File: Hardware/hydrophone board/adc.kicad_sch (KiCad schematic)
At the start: 25 parts, among them J301 Conn_01x08

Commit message: changed all cap + resistors to 0805, starting filter layout
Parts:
- C301, C302, C303, C305, C306, C308, C309, C310, C311, C312, C313, C314, C315, C316, C317, C318: footprint Capacitor_SMD:C_0603_1608Metric -> Capacitor_SMD:C_0805_2012Metric_Pad1.18x1.45mm_HandSolder
- C304, C307: footprint Capacitor_SMD:C_0805_2012Metric -> Capacitor_SMD:C_0805_2012Metric_Pad1.18x1.45mm_HandSolder
- R301, R302, R303, R304, R305: footprint Resistor_SMD:R_0603_1608Metric -> Resistor_SMD:R_0805_2012Metric_Pad1.20x1.40mm_HandSolder
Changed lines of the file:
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@@
       (effects (font (size 1.27 1.27)))
     )
-    (property "Footprint" "Capacitor_SMD:C_0603_1608Metric" (at 118.11 176.8348 0)
+    (property "Footprint" "Capacitor_SMD:C_0805_2012Metric_Pad1.18x1.45mm_HandSolder" (at 118.11 176.8348 0)
       (effects (font (size 1.27 1.27)) hide)
     )
@@
       (effects (font (size 1.27 1.27)) (justify left))
     )
-    (property "Footprint" "Capacitor_SMD:C_0603_1608Metric" (at 38.1 49.53 0)
+    (property "Footprint" "Capacitor_SMD:C_0805_2012Metric_Pad1.18x1.45mm_HandSolder" (at 38.1 49.53 0)
       (effects (font (size 1.27 1.27)) hide)
     )
@@
       (effects (font (size 1.27 1.27)) (justify left))
     )
-    (property "Footprint" "Resistor_SMD:R_0603_1608Metric" (at 242.316 101.854 90)
+    (property "Footprint" "Resistor_SMD:R_0805_2012Metric_Pad1.20x1.40mm_HandSolder" (at 242.316 101.854 90)
       (effects (font (size 1.27 1.27)) hide)
     )
@@
       (effects (font (size 1.27 1.27)) (justify left))
     )
-    (property "Footprint" "Capacitor_SMD:C_0603_1608Metric" (at 77.1652 53.34 0)
+    (property "Footprint" "Capacitor_SMD:C_0805_2012Metric_Pad1.18x1.45mm_HandSolder" (at 77.1652 53.34 0)
       (effects (font (size 1.27 1.27)) hide)
     )
@@
     (pin "18")
     (pin "19")
-    (pin "2")
     (pin "20")
     (pin "21")
@@
     (pin "8")
     (pin "9")
+    (pin "2")
     (instances
       (project "hydrophone board"
@@
       (effects (font (size 1.27 1.27)) (justify right))
     )
-    (property "Footprint" "Resistor_SMD:R_0603_1608Metric" (at 189.484 106.426 90)
+    (property "Footprint" "Resistor_SMD:R_0805_2012Metric_Pad1.20x1.40mm_HandSolder" (at 189.484 106.426 90)
       (effects (font (size 1.27 1.27)) hide)
     )
@@
       (effects (font (size 1.27 1.27)))
     )
-    (property "Footprint" "Capacitor_SMD:C_0603_1608Metric" (at 54.61 176.8348 0)
+    (property "Footprint" "Capacitor_SMD:C_0805_2012Metric_Pad1.18x1.45mm_HandSolder" (at 54.61 176.8348 0)
       (effects (font (size 1.27 1.27)) hide)
     )
@@
       (effects (font (size 1.27 1.27)) (justify left))
     )
-    (property "Footprint" "Capacitor_SMD:C_0603_1608Metric" (at 214.3252 64.77 0)
+    (property "Footprint" "Capacitor_SMD:C_0805_2012Metric_Pad1.18x1.45mm_HandSolder" (at 214.3252 64.77 0)
       (effects (font (size 1.27 1.27)) hide)
     )
@@
       (effects (font (size 1.27 1.27)) (justify left))
     )
-    (property "Footprint" "Capacitor_SMD:C_0603_1608Metric" (at 239.7252 57.15 0)
+    (property "Footprint" "Capacitor_SMD:C_0805_2012Metric_Pad1.18x1.45mm_HandSolder" (at 239.7252 57.15 0)
       (effects (font (size 1.27 1.27)) hide)
     )
@@
       (effects (font (size 1.27 1.27)) (justify left))
     )
-    (property "Footprint" "Resistor_SMD:R_0603_1608Metric" (at 204.216 106.934 90)
+    (property "Footprint" "Resistor_SMD:R_0805_2012Metric_Pad1.20x1.40mm_HandSolder" (at 204.216 106.934 90)
       (effects (font (size 1.27 1.27)) hide)
     )
@@
       (effects (font (size 1.27 1.27)))
     )
-    (property "Footprint" "Capacitor_SMD:C_0603_1608Metric" (at 118.11 164.1348 0)
+    (property "Footprint" "Capacitor_SMD:C_0805_2012Metric_Pad1.18x1.45mm_HandSolder" (at 118.11 164.1348 0)
       (effects (font (size 1.27 1.27)) hide)
     )
@@
       (effects (font (size 1.27 1.27)))
     )
-    (property "Footprint" "Capacitor_SMD:C_0603_1608Metric" (at 54.61 126.0348 0)
+    (property "Footprint" "Capacitor_SMD:C_0805_2012Metric_Pad1.18x1.45mm_HandSolder" (at 54.61 126.0348 0)
       (effects (font (size 1.27 1.27)) hide)
     )
@@
       (effects (font (size 1.27 1.27)))
     )
-    (property "Footprint" "Capacitor_SMD:C_0603_1608Metric" (at 54.61 164.1348 0)
+    (property "Footprint" "Capacitor_SMD:C_0805_2012Metric_Pad1.18x1.45mm_HandSolder" (at 54.61 164.1348 0)
       (effects (font (size 1.27 1.27)) hide)
     )
@@
       (effects (font (size 1.27 1.27)))
     )
-    (property "Footprint" "Capacitor_SMD:C_0603_1608Metric" (at 118.11 138.7348 0)
+    (property "Footprint" "Capacitor_SMD:C_0805_2012Metric_Pad1.18x1.45mm_HandSolder" (at 118.11 138.7348 0)
       (effects (font (size 1.27 1.27)) hide)
     )
@@
       (effects (font (size 1.27 1.27)) (justify left))
     )
-    (property "Footprint" "Capacitor_SMD:C_0603_1608Metric" (at 51.7652 53.34 0)
+    (property "Footprint" "Capacitor_SMD:C_0805_2012Metric_Pad1.18x1.45mm_HandSolder" (at 51.7652 53.34 0)
       (effects (font (size 1.27 1.27)) hide)
     )
@@
       (effects (font (size 1.27 1.27)) (justify left))
     )
-    (property "Footprint" "Capacitor_SMD:C_0603_1608Metric" (at 26.3652 53.34 0)
+    (property "Footprint" "Capacitor_SMD:C_0805_2012Metric_Pad1.18x1.45mm_HandSolder" (at 26.3652 53.34 0)
       (effects (font (size 1.27 1.27)) hide)
     )
@@
       (effects (font (size 1.27 1.27)))
     )
-    (property "Footprint" "Capacitor_SMD:C_0603_1608Metric" (at 118.11 126.0348 0)
+    (property "Footprint" "Capacitor_SMD:C_0805_2012Metric_Pad1.18x1.45mm_HandSolder" (at 118.11 126.0348 0)
       (effects (font (size 1.27 1.27)) hide)
     )
@@
       (effects (font (size 1.27 1.27)) (justify left))
     )
-    (property "Footprint" "Resistor_SMD:R_0603_1608Metric" (at 229.616 101.854 90)
+    (property "Footprint" "Resistor_SMD:R_0805_2012Metric_Pad1.20x1.40mm_HandSolder" (at 229.616 101.854 90)
       (effects (font (size 1.27 1.27)) hide)
     )
@@
       (effects (font (size 1.27 1.27)) (justify left))
     )
-    (property "Footprint" "Capacitor_SMD:C_0805_2012Metric" (at 251.46 53.34 0)
+    (property "Footprint" "Capacitor_SMD:C_0805_2012Metric_Pad1.18x1.45mm_HandSolder" (at 251.46 53.34 0)
       (effects (font (size 1.27 1.27)) hide)
     )
@@
       (effects (font (size 1.27 1.27)))
     )
-    (property "Footprint" "Capacitor_SMD:C_0603_1608Metric" (at 54.61 138.7348 0)
+    (property "Footprint" "Capacitor_SMD:C_0805_2012Metric_Pad1.18x1.45mm_HandSolder" (at 54.61 138.7348 0)
       (effects (font (size 1.27 1.27)) hide)
     )
@@
       (effects (font (size 1.27 1.27)) (justify left))
     )
-    (property "Footprint" "Capacitor_SMD:C_0805_2012Metric" (at 63.5 49.53 0)
+    (property "Footprint" "Capacitor_SMD:C_0805_2012Metric_Pad1.18x1.45mm_HandSolder" (at 63.5 49.53 0)
       (effects (font (size 1.27 1.27)) hide)
     )
@@
       (effects (font (size 1.27 1.27)) (justify left))
     )
-    (property "Footprint" "Resistor_SMD:R_0603_1608Metric" (at 199.644 151.384 90)
+    (property "Footprint" "Resistor_SMD:R_0805_2012Metric_Pad1.20x1.40mm_HandSolder" (at 199.644 151.384 90)
       (effects (font (size 1.27 1.27)) hide)
     )
@@
       (effects (font (size 1.27 1.27)) (justify left))
     )
-    (property "Footprint" "Capacitor_SMD:C_0603_1608Metric" (at 226.06 60.96 0)
+    (property "Footprint" "Capacitor_SMD:C_0805_2012Metric_Pad1.18x1.45mm_HandSolder" (at 226.06 60.96 0)
       (effects (font (size 1.27 1.27)) hide)
     )
@@
       (effects (font (size 1.27 1.27)))
     )
-    (property "Footprint" "Capacitor_SMD:C_0603_1608Metric" (at 92.71 56.8452 0)
-      (effects (font (size 1.27 1.27)) hide)
-    )
+    (property "Footprint" "Capacitor_SMD:C_0805_2012Metric_Pad1.18x1.45mm_HandSolder" (at 92.71 56.8452 0)
+      (effects (font (size 1.27 1.27)) hide)
+    )

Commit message: changed some aprts
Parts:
- removed J301: Conn_01x08, Connector_PinSocket_2.54mm:PinSocket_1x08_P2.54mm_Vertical, symbol Connector_Generic:Conn_01x08
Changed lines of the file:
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@@
-    (stroke (width 0) (type default))
-  )
-  (wire (pts (xy 63.5 101.6) (xy 68.58 101.6))
     (stroke (width 0) (type default))
   )
@@
     (stroke (width 0) (type default))
   )
-  (wire (pts (xy 63.5 88.9) (xy 68.58 88.9))
-    (stroke (width 0) (type default))
-  )
   (wire (pts (xy 241.3 95.25) (xy 241.3 97.79))
     (stroke (width 0) (type default))
@@
     (stroke (width 0) (type default))
   )
-  (wire (pts (xy 63.5 96.52) (xy 68.58 96.52))
-    (stroke (width 0) (type default))
-  )
   (wire (pts (xy 228.6 105.41) (xy 228.6 114.3))
     (stroke (width 0) (type default))
@@
     (stroke (width 0) (type default))
   )
-  (wire (pts (xy 63.5 91.44) (xy 68.58 91.44))
-    (stroke (width 0) (type default))
-  )
   (wire (pts (xy 185.42 64.77) (xy 193.04 64.77))
     (stroke (width 0) (type default))
   )
-  (wire (pts (xy 63.5 99.06) (xy 68.58 99.06))
-    (stroke (width 0) (type default))
-  )
   (wire (pts (xy 191.77 152.4) (xy 195.58 152.4))
     (stroke (width 0) (type default))
@@
     (stroke (width 0) (type default))
   )
-  (wire (pts (xy 63.5 93.98) (xy 68.58 93.98))
-    (stroke (width 0) (type default))
-  )
-  (wire (pts (xy 63.5 106.68) (xy 68.58 106.68))
-    (stroke (width 0) (type default))
-  )
   (wire (pts (xy 118.11 165.1) (xy 127 165.1))
     (stroke (width 0) (type default))
@@
   )
   (wire (pts (xy 228.6 90.17) (xy 228.6 95.25))
-    (stroke (width 0) (type default))
-  )
-  (wire (pts (xy 63.5 104.14) (xy 68.58 104.14))
     (stroke (width 0) (type default))
   )
@@
     (effects (font (size 1.27 1.27)) (justify right bottom))
   )
-  (label "IN1P" (at 68.58 88.9 0) (fields_autoplaced)
-    (effects (font (size 1.27 1.27)) (justify left bottom))
-  )
   (label "SDA" (at 191.77 57.15 180) (fields_autoplaced)
     (effects (font (size 1.27 1.27)) (justify right bottom))
@@
     (effects (font (size 1.27 1.27)) (justify left bottom))
   )
-  (label "IN4M" (at 68.58 106.68 0) (fields_autoplaced)
-    (effects (font (size 1.27 1.27)) (justify left bottom))
-  )
-  (label "IN1M" (at 68.58 91.44 0) (fields_autoplaced)
-    (effects (font (size 1.27 1.27)) (justify left bottom))
-  )
   (label "IN3M" (at 114.3 64.77 0) (fields_autoplaced)
     (effects (font (size 1.27 1.27)) (justify left bottom))
@@
     (effects (font (size 1.27 1.27)) (justify right bottom))
   )
-  (label "IN2P" (at 68.58 93.98 0) (fields_autoplaced)
-    (effects (font (size 1.27 1.27)) (justify left bottom))
-  )
   (label "SCL" (at 241.3 110.49 90) (fields_autoplaced)
     (effects (font (size 1.27 1.27)) (justify left bottom))
@@
     (effects (font (size 1.27 1.27)) (justify left bottom))
   )
-  (label "IN3M" (at 68.58 101.6 0) (fields_autoplaced)
-    (effects (font (size 1.27 1.27)) (justify left bottom))
-  )
   (label "SCL" (at 191.77 59.69 180) (fields_autoplaced)
     (effects (font (size 1.27 1.27)) (justify right bottom))
   )
-  (label "IN2M" (at 68.58 96.52 0) (fields_autoplaced)
-    (effects (font (size 1.27 1.27)) (justify left bottom))
-  )
   (label "IN3M" (at 127 139.7 180) (fields_autoplaced)
     (effects (font (size 1.27 1.27)) (justify right bottom))
@@
     (effects (font (size 1.27 1.27)) (justify right bottom))
   )
-  (label "IN4P" (at 68.58 104.14 0) (fields_autoplaced)
-    (effects (font (size 1.27 1.27)) (justify left bottom))
-  )
   (label "IN4P" (at 127 165.1 180) (fields_autoplaced)
     (effects (font (size 1.27 1.27)) (justify right bottom))
@@
   )
   (label "SHDNZ" (at 207.01 152.4 0) (fields_autoplaced)
-    (effects (font (size 1.27 1.27)) (justify left bottom))
-  )
-  (label "IN3P" (at 68.58 99.06 0) (fields_autoplaced)
     (effects (font (size 1.27 1.27)) (justify left bottom))
   )
@@
         )
       )
-    )
-  )
-  (symbol (lib_id "Connector_Generic:Conn_01x08") (at 58.42 99.06 180) (unit 1)
-    (in_bom yes) (on_board yes) (dnp no) (fields_autoplaced)
-    (property "Reference" "J301" (at 58.42 83.82 0)
-      (effects (font (size 1.27 1.27)))
-    )
-    (property "Value" "Conn_01x08" (at 58.42 86.36 0)
-      (effects (font (size 1.27 1.27)))
-    )
-    (property "Footprint" "Connector_PinSocket_2.54mm:PinSocket_1x08_P2.54mm_Vertical" (at 58.42 99.06 0)
-      (effects (font (size 1.27 1.27)) hide)
-    )
-    (property "Datasheet" "~" (at 58.42 99.06 0)
-      (effects (font (size 1.27 1.27)) hide)
-    )
-    (pin "1")
-    (pin "2")
-    (pin "3")
-    (pin "4")
-    (pin "5")
-    (pin "6")
-    (pin "7")
-    (pin "8")
-    (instances
-      (project "hydrophone board"
-        (path "/4356d3a6-6a00-447d-897e-473f60221539/c9760799-658d-4181-af96-8731ebbcaea9"
-          (reference "J301") (unit 1)
-        )
-      )

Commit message: BOM things
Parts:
- R301, R302: value 2k -> 2.2k
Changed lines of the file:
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@@
       (effects (font (size 1.27 1.27)) (justify left))
     )
-    (property "Value" "2k" (at 243.84 103.505 0)
+    (property "Value" "2.2k" (at 243.84 103.505 0)
       (effects (font (size 1.27 1.27)) (justify left))
     )
@@
       (effects (font (size 1.27 1.27)) (justify left))
     )
-    (property "Value" "2k" (at 231.14 103.505 0)
-      (effects (font (size 1.27 1.27)) (justify left))
-    )
+    (property "Value" "2.2k" (at 231.14 103.505 0)
+      (effects (font (size 1.27 1.27)) (justify left))
+    )

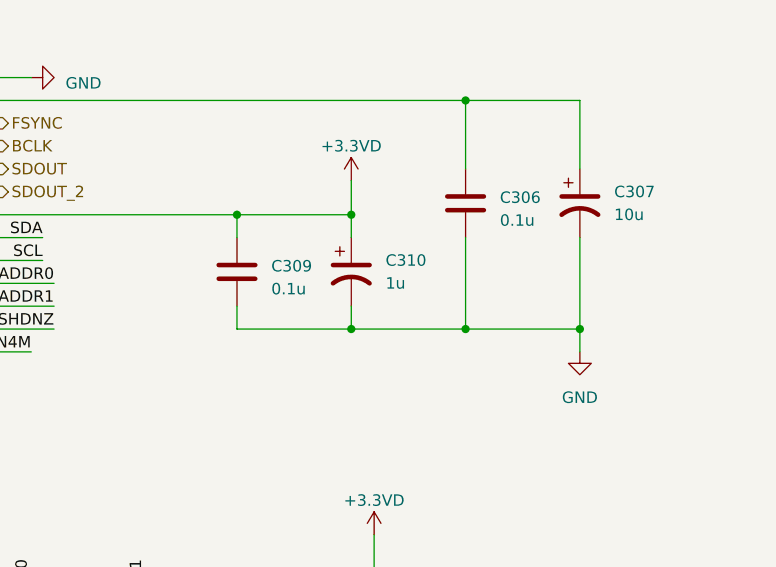
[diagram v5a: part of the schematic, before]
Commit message: changed iovdd cap, thermal pad via size
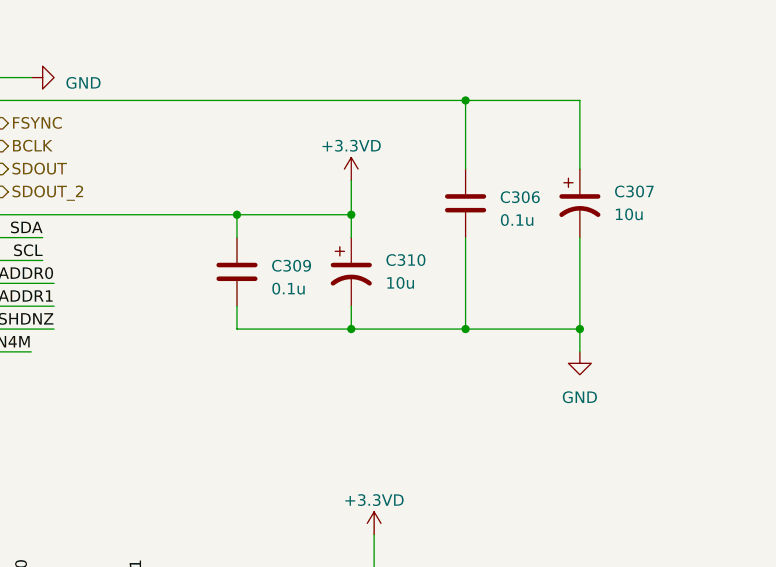
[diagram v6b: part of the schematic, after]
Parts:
- C310: value 1u -> 10u
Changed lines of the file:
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@@
       (effects (font (size 1.27 1.27)) (justify left))
     )
-    (property "Value" "1u" (at 229.87 62.23 0)
+    (property "Value" "10u" (at 229.87 62.23 0)
       (effects (font (size 1.27 1.27)) (justify left))
     )
